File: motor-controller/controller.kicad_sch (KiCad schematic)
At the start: 20 parts

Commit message: Update controller.kicad_sch
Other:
- note added: "Case Temp Sensor"
- note added: "PWM INPUT"
- note added: "RGB LED"
- moved on the sheet: C?, J?, R?, TP?, U?

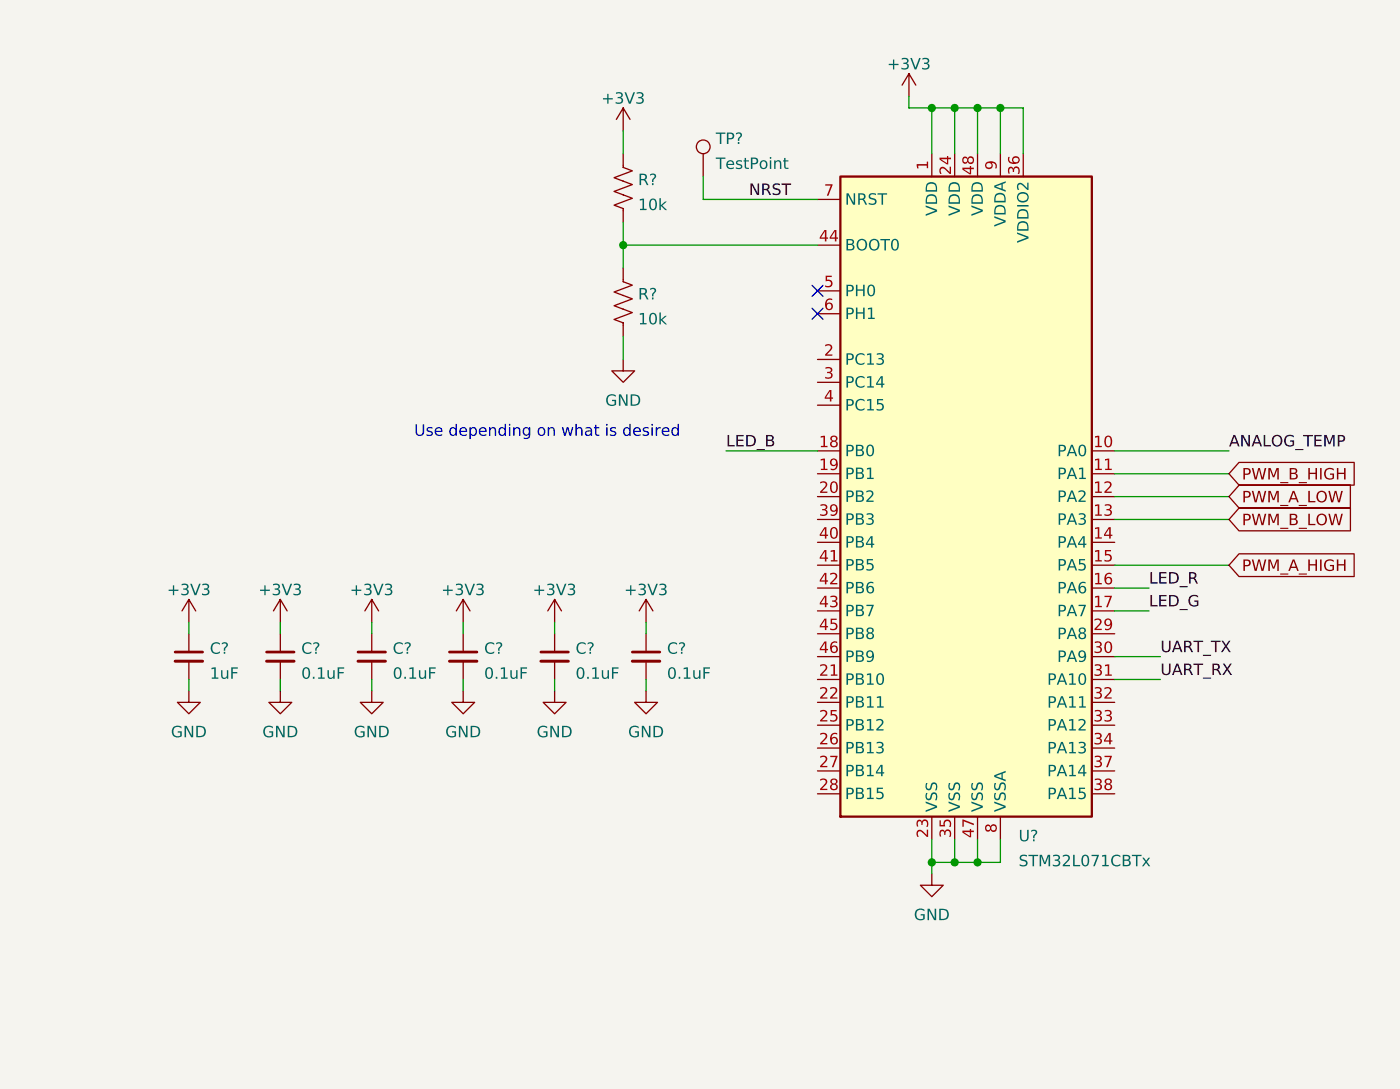
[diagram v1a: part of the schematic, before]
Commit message: Remove MCU stuff
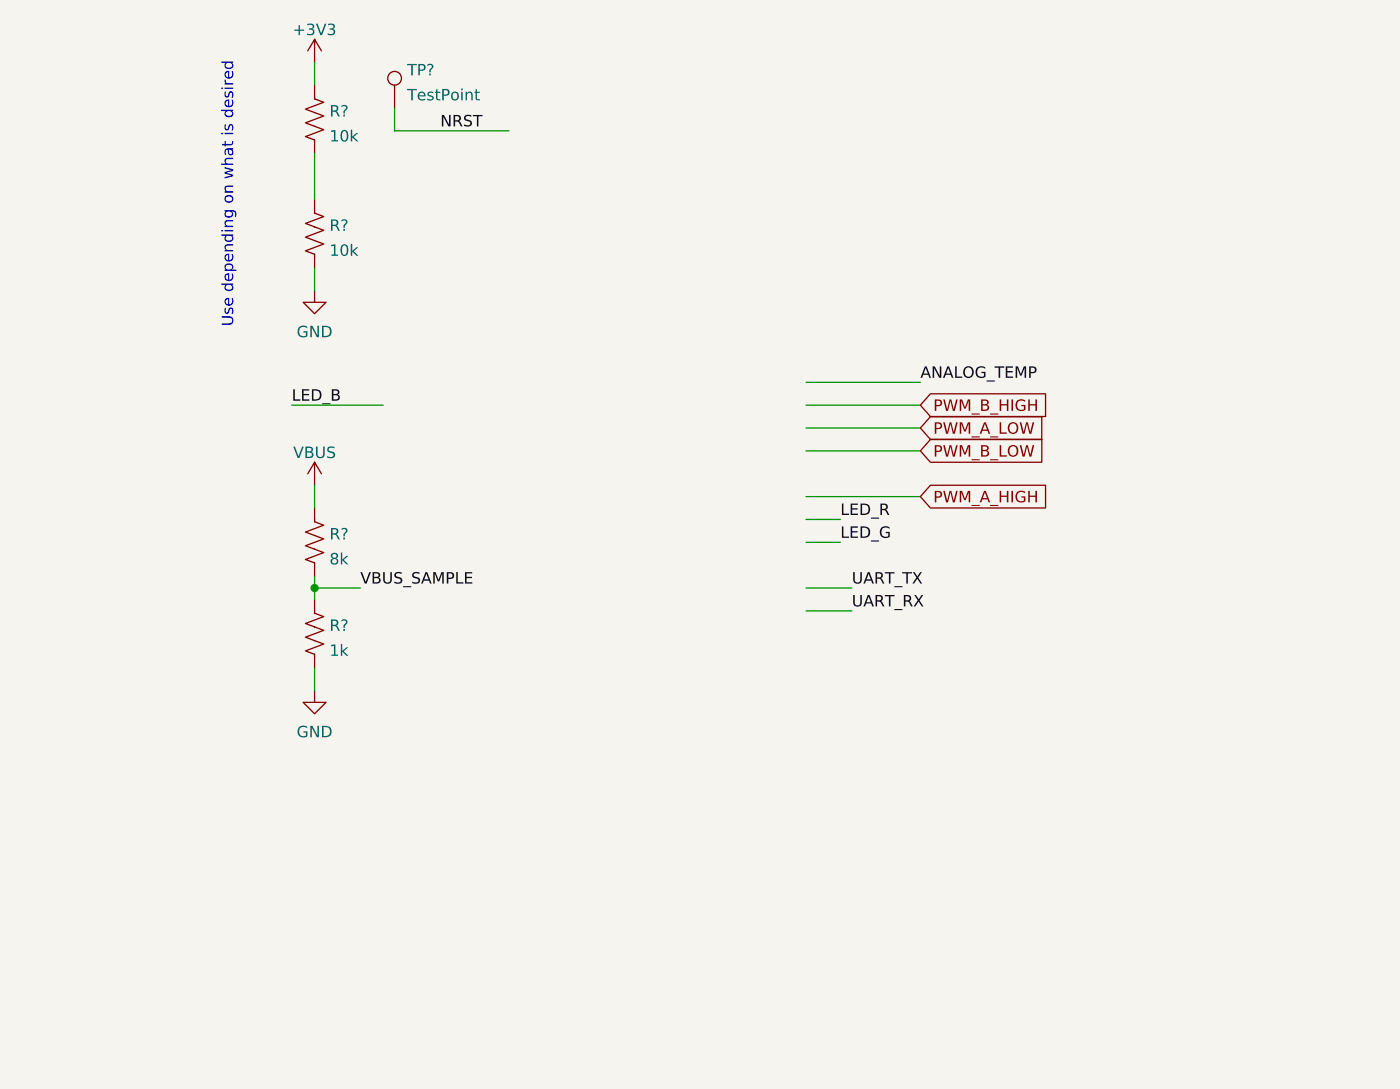
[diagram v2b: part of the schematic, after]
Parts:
- removed C?: 1uF, symbol Device:C_Small
- removed C? (x5): 0.1uF, symbol Device:C_Small
- removed U?: STM32L071CBTx, Package_QFP:LQFP-48_7x7mm_P0.5mm, symbol MCU_ST_STM32L0:STM32L071CBTx
- added R?: 8k, symbol Device:R_US
- added R?: 1k, symbol Device:R_US
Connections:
- net GND: now also R?.2
- new net VBUS: R?.1
- new net VBUS_SAMPLE: R?.1, R?.2
- no-connect marks 2 -> 0
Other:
- moved on the sheet: R?, TP?

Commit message: MCU Upload
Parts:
- added J?: Conn_01x04, Connector:FanPinHeader_1x04_P2.54mm_Vertical, symbol Connector_Generic:Conn_01x04
- added J?: Screw_Terminal_01x02, TerminalBlock:TerminalBlock_bornier-2_P5.08mm, symbol Connector:Screw_Terminal_01x02
- added U?: L7805CV, digikey-footprints:TO-220-3, symbol dk_PMIC-Voltage-Regulators-Linear:L7805CV
- added U?: STM32G030F6P6TR, STMicroelectronics-TSSOP20-YA-0-3-*, symbol eec:STM32G030F6P6TR
- added U?: LD1117V33, digikey-footprints:TO-220-3, symbol dk_PMIC-Voltage-Regulators-Linear:LD1117V33
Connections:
- net +3V3: now also J?.4 (Pin_4), U?.2 (VOUT), U?.4 (VDD/VDDA), U?.5 (VSS/VSSA)
- net +5V: now also U?.3 (OUT), U?.3 (VIN)
- net ANALOG_TEMP: now also U?.7 (PA0)
- net GND: now also J?.1 (Pin_1), J?.3 (Pin_3), U?.1 (GND), U?.2 (GND)
- net LED_B: now also U?.20 (PB3/PB4/PB5/PB6)
- net LED_G: now also U?.16 (PA11[PA9])
- net LED_R: now also U?.15 (PB0/PB1/PB2/PA8)
- net NRST: now also U?.6 (~{RST})
- net PWM_A_HIGH: now also U?.14 (PA7)
- net PWM_A_LOW: now also U?.12 (PA5)
- net PWM_B_HIGH: now also U?.13 (PA6)
- net PWM_B_LOW: now also U?.17 (PA12[PA10])
- net PWM_IN: now also U?.11 (PA4)
- net UART_RX: now also U?.10 (PA3)
- net UART_TX: now also U?.9 (PA2)
- net VBUS: now also J?.2 (Pin_2), U?.1 (IN)
- net VBUS_SAMPLE: now also U?.8 (PA1)
- new net SWCLK: J?.2 (Pin_2), U?.19 (PA15/PA14-BOOT0)
- new net SWDIO: J?.1 (Pin_1), U?.18 (PA13)
- no-connect marks 0 -> 3
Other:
- note added: "Add Capacitor Here"
- note added: "Are these decoupling?"
- note added: "CODE UPLOAD"
- note added: "No external oscillator used"
- note added: "STM32 MCU"
- note added: "TODO: REPLACE WITH TERMINAL BLOCK"
- note added: "VBUS"
- note added: "VOLTAGE REGULATION"
- note added: "Voltage Monitoring"
- moved on the sheet: R?, TP?

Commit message: Test Commit
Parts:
- removed J?: Screw_Terminal_01x02, TerminalBlock:TerminalBlock_bornier-2_P5.08mm, symbol Connector:Screw_Terminal_01x02
- removed R? (x3): 1k, symbol Device:R_US
- removed U?: L7805CV, digikey-footprints:TO-220-3, symbol dk_PMIC-Voltage-Regulators-Linear:L7805CV
- removed U?: LD1117V33, digikey-footprints:TO-220-3, symbol dk_PMIC-Voltage-Regulators-Linear:LD1117V33
- added C? (x2): 10uF, symbol Device:C_Small
- added C?: 0.1uF, symbol Device:C_Small
- added C?: 0.47uF, symbol Device:C_Small
- added C?: 22uF, symbol Device:C_Small
- added D? (x2): PWR LED, symbol Device:LED
- added R? (x2): 1k, symbol Device:R_US
- added U?: NCP1117ST33T3G, digikey-footprints:SOT-223, symbol dk_PMIC-Voltage-Regulators-Linear:NCP1117ST33T3G
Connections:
- net +3V3: now also C?.1, R?.1, U?.2 (OUT), U?.4 (OUT); no longer U?.5 (VSS/VSSA)
- net +5V: now also C?.1, C?.1, R?.1, U?.3 (IN)
- net GND: now also U?.5 (VSS/VSSA), C?.2, C?.2, C?.2, C?.2, C?.2, D?.1 (K), D?.1 (K), U?.1 (ADJ/GND)
- net NRST: now also C?.1
- net PWM_IN: now also J?.3 (Pin_3), TP?.1
- net VBUS: now also C?.1
- new net: D?.2 (A), R?.2 (x2)
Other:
- note added: "DECOUPLING CAPS"
- note added: "LM2940 HERE"
- note added: "POWER LEDS"
- note added: "TODO: CHECK IF 3.3V CAPS NEED TO BE POLARIZED"
- note added: "TODO: Figure out values of decoupling"
- note added: "TODO: Figure out values of power LEDs"
- note removed: "TODO: REPLACE WITH TERMINAL BLOCK"
- note removed: "VBUS"
- moved on the sheet: D?, J?, R?
